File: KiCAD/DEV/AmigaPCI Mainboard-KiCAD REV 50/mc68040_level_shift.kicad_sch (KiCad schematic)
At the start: 28 parts, among them U801 74LVC1G17, U802 SN74LVC16T245DLR, U803 SN74LVC16T245DLR, U804 SN74LVC16T245DLR, U805 SN74LVC16T245DLR, U806 74LVC245, U807 74LVC245, U808 74LVC245, U809 74LVC245, U810 SN74LVC16T245DLR

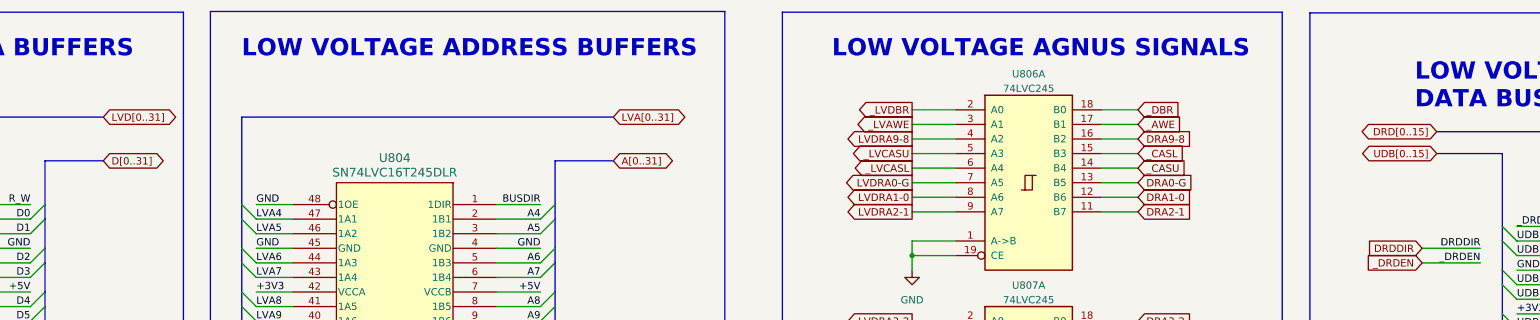
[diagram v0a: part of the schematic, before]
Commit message: Updated STM32F205 microcontroller.
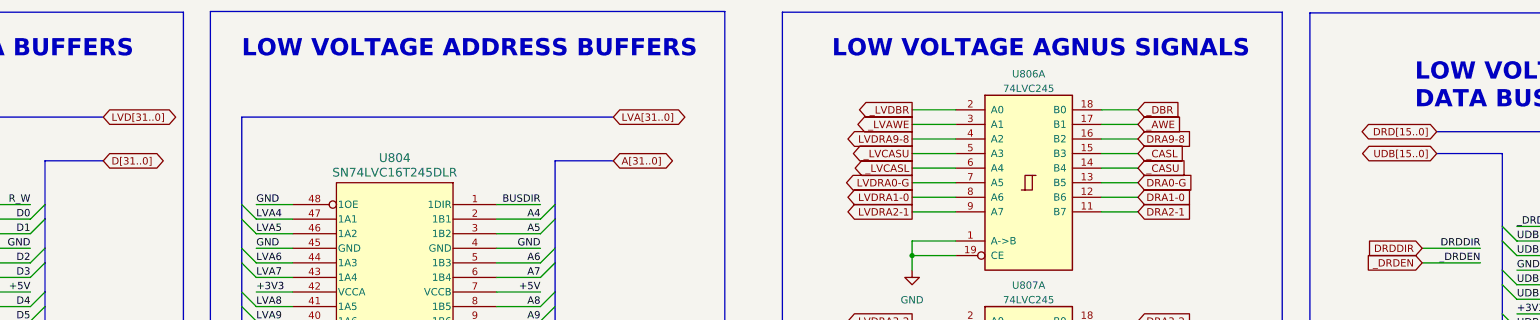
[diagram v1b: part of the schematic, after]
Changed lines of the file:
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@@
 		)
 	)
-	(global_label "LVD[0..31]"
+	(global_label "LVD[31..0]"
 		(shape bidirectional)
 		(at 93.98 35.56 0)
@@
 		)
 	)
-	(global_label "A[0..31]"
+	(global_label "A[31..0]"
 		(shape bidirectional)
 		(at 182.88 43.18 0)
@@
 		)
 	)
-	(global_label "LVA[0..31]"
+	(global_label "LVA[31..0]"
 		(shape bidirectional)
 		(at 182.88 35.56 0)
@@
 		)
 	)
-	(global_label "UDB[0..15]"
+	(global_label "UDB[15..0]"
 		(shape bidirectional)
 		(at 326.39 41.91 180)
@@
 		)
 	)
-	(global_label "D[0..31]"
+	(global_label "D[31..0]"
 		(shape bidirectional)
 		(at 93.98 43.18 0)
@@
 		)
 	)
-	(global_label "DRD[0..15]"
+	(global_label "DRD[15..0]"
 		(shape bidirectional)
 		(at 326.39 38.1 180)

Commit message: More Rev 5.0 updates.
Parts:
- removed C801: 0.1uF, Capacitor_SMD:C_0603_1608Metric, symbol Device:C_Small
- removed U801: 74LVC1G17, Package_TO_SOT_SMD:SOT-23-5, symbol 74xGxx:74LVC1G17
- removed U810: SN74LVC16T245DLR, AmigaPCI:48-BSSOP, symbol AmigaPCI-Symbols:SN74LVC16T245DLR
- added U231: 74LVC08, Package_SO:TSSOP-14_4.4x5mm_P0.65mm, symbol 74xx:74LS08
- added U810: 74LVC16646, Package_SO:SSOP-56_7.5x18.5mm_P0.635mm, symbol AmigaPCI-Symbols:74LVC16646
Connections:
- net +3V3: now also C824.1, C825.1, U231.12, U810.22 (VCC), U810.35 (VCC), U810.50 (VCC), U810.7 (VCC)
- net +5V: no longer C824.1, C825.1
- net DRD0: now also U810.52 (1B1)
- net DRD1: now also U810.51 (1B2)
- net DRD10: now also U810.40 (2B3)
- net DRD11: now also U810.38 (2B4)
- net DRD12: now also U810.37 (2B5)
- net DRD13: now also U810.36 (2B6)
- net DRD14: now also U810.34 (2B7)
- net DRD15: now also U810.33 (2B8)
- net DRD2: now also U810.49 (1B3)
- net DRD3: now also U810.48 (1B4)
- net DRD4: now also U810.47 (1B5)
- net DRD5: now also U810.45 (1B6)
- net DRD6: now also U810.44 (1B7)
- net DRD7: now also U810.43 (1B8)
- net DRD8: now also U810.42 (2B1)
- net DRD9: now also U810.41 (2B2)
- net DRDDIR: now also U810.1 (1DIR), U810.28 (2DIR)
- net GND: now also U810.11 (GND), U810.18 (GND), U810.25 (GND), U810.30 (2CLKBA), U810.31 (2SBA), U810.32 (GND), U810.39 (GND), U810.4 (GND), U810.46 (GND), U810.53 (GND), U810.54 (1SBA), U810.55 (1CLKBA)
- net UDB0: now also U810.5 (1A1)
- net UDB1: now also U810.6 (1A2)
- net UDB10: now also U810.17 (2A3)
- net UDB11: now also U810.19 (2A4)
- net UDB12: now also U810.20 (2A5)
- net UDB13: now also U810.21 (2A6)
- net UDB14: now also U810.23 (2A7)
- net UDB15: now also U810.24 (2A8)
- net UDB2: now also U810.8 (1A3)
- net UDB3: now also U810.9 (1A4)
- net UDB4: now also U810.10 (1A5)
- net UDB5: now also U810.12 (1A6)
- net UDB6: now also U810.13 (1A7)
- net UDB7: now also U810.14 (1A8)
- net UDB8: now also U810.15 (2A1)
- net UDB9: now also U810.16 (2A2)
- net _BR: now also U231.13
- net _DRDEN: now also U810.29 (*2OE), U810.56 (*1OE)
- net _LVBR: now also U231.11
- net _LVCASL: now also U806.5 (A3); no longer U806.6 (A4)
- net _LVCASU: now also U806.6 (A4); no longer U806.5 (A3)
- net _LVRAS0: now also U807.9 (A7); no longer U807.8 (A6)
- net _LVRAS1: now also U807.8 (A6); no longer U807.9 (A7)
- new net DMALATCH: U810.26 (2SAB), U810.3 (1SAB)
- new net LATCHCLK: U810.2 (1CLKAB), U810.27 (2CLKAB)
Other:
- note added: "BUS REQUEST"
- note added: "DMA READ = ENABLED, LATCHED, DIR = 1 (A>B) DMA WRITE = ENABLED, LIVE, DIR = 0 (B>A) REG READ = ENABLED, LIVE, DIR = 0 (B>A) REG WRITE = ENABLED, LIVE, DIR = 1 (A>B) CPU CHIP RAM ACCESS = TRISTATE"
- note added: "LOW VOLTAGE CHIPSET RAM DATA BUS BUFFER/LATCH"
- note removed: "DMA READ = ENABLED, DIR = 1 (A>B) DMA WRITE = ENABLED, DIR = 0 (B>A) REG READ = ENABLED, DIR = 0 (B>A) REG WRITE = ENABLED, DIR = 1 (A>B) CPU CHIP RAM ACCESS = TRISTATE"
- note removed: "LOW VOLTAGE CHIPSET RAM DATA BUS BUFFERS"
- note removed: "UNIDIRECTIONAL SIGNALS"
- moved on the sheet: C814, C815, C824, C825
